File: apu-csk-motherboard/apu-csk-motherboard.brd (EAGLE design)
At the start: 90.2 x 95.9 mm, 9 parts

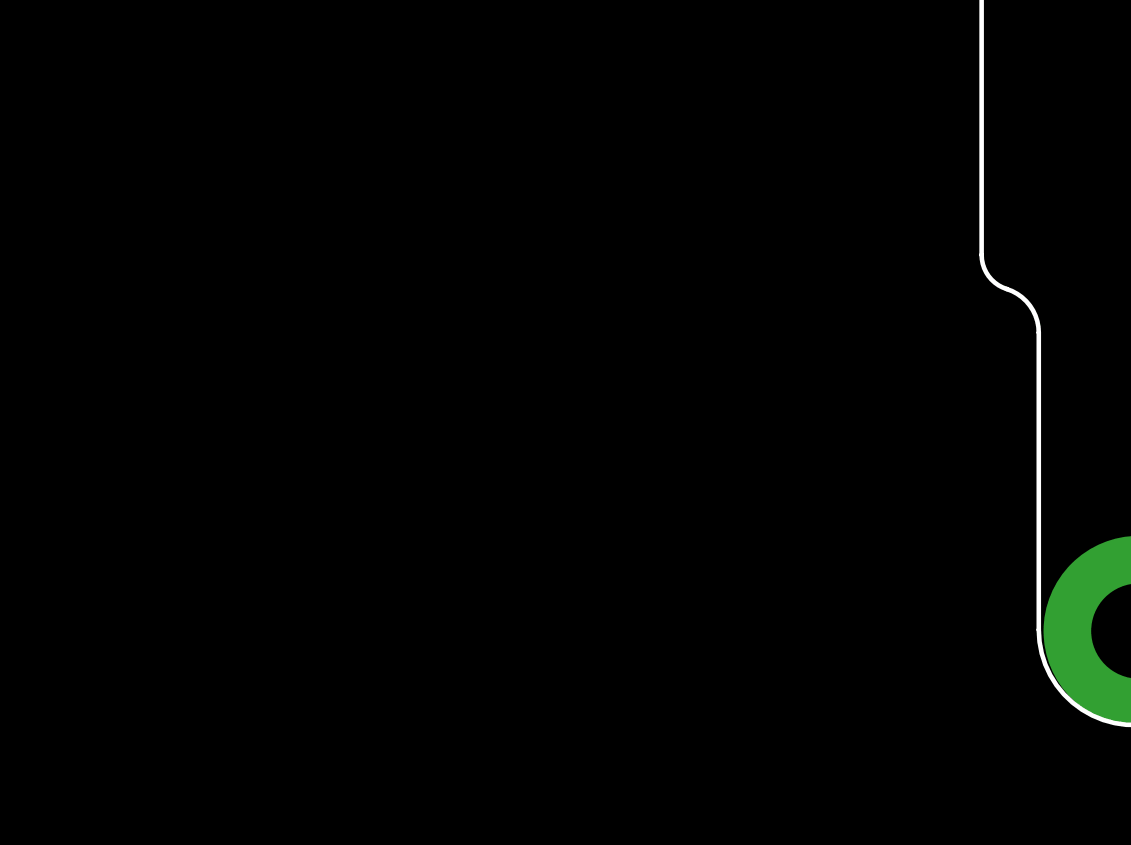
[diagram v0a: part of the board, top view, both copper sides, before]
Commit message: added the sd card schematic to the library
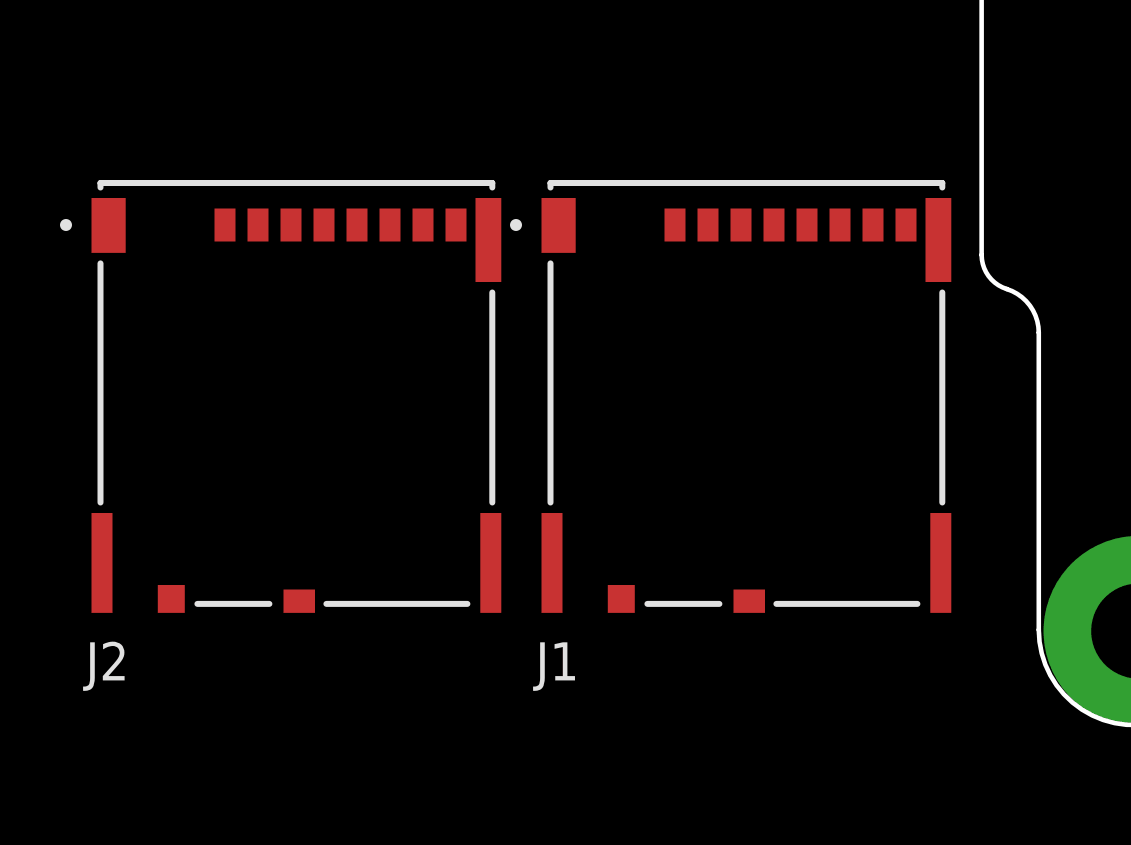
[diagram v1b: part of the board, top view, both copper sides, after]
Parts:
- added J1, J2: MEM2080-00-128-00-A_REVA, MEM2080-00-128-00-A_REVA:GCT_MEM2080-00-128-00-A_REVA
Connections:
- new net VDD: J1.P4, J2.P4
- new net VSS: J1.P6, J2.P6
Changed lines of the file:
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@@
 </layers>
 <board>
-<fusionsync huburn="a.cGVyc29uYWw6dWUyZDI2NzMx" projecturn="a.cGVyc29uYWw6dWUyZDI2NzMxIzIwMjIwOTMwNTYyNjE0OTA2" f3durn="urn:adsk.wipprod:dm.lineage:kB2Wh1Q4TRikTqmI8AqMMA" pcbguid="" lastpulledtime="" lastsyncedchangeguid="" latestrevisionid="4b27a098-c4a4-4352-931e-bf35d80debb3" lastsyncedrevisionid="4b27a098-c4a4-4352-931e-bf35d80debb3" lastboardhashguid="35456882-ee58-db46-62f4-8c871885f9ca" lastpushedtime="2022-10-02T03:41:01Z" linktopcb3d="true"/>
+<fusionsync huburn="a.cGVyc29uYWw6dWUyZDI2NzMx" projecturn="a.cGVyc29uYWw6dWUyZDI2NzMxIzIwMjIwOTMwNTYyNjE0OTA2" f3durn="urn:adsk.wipprod:dm.lineage:kB2Wh1Q4TRikTqmI8AqMMA" pcbguid="" lastpulledtime="" lastsyncedchangeguid="" latestrevisionid="4b27a098-c4a4-4352-931e-bf35d80debb3" lastsyncedrevisionid="4b27a098-c4a4-4352-931e-bf35d80debb3" lastboardhashguid="35456882-ee58-db46-62f4-8c871885f9ca" lastpushedtime="2022-10-02T03:41:01Z" linktopcb3d="false"/>
 <plain>
 <wire x1="39.9699" y1="4.4855" x2="41.4939" y2="2.9615" width="0.1524" layer="20" curve="90" locked="yes"/>
@@
 <attribute name="VALUE" x="0" y="55.75" locked="yes" size="1.27" layer="27"/>
 </element>
+<element name="J1" library="MEM2080-00-128-00-A_REVA" package="GCT_MEM2080-00-128-00-A_REVA" value="MEM2080-00-128-00-A_REVA" x="-8" y="13" smashed="yes">
+<attribute name="AVAILABILITY" value="In Stock" x="-8" y="13" size="1.778" layer="27" display="off"/>
+<attribute name="DESCRIPTION" value=" 9 (8 + 1) Position Card Connector Secure Digital - microSD™ Surface Mount, Right Angle Gold " x="-8" y="13" size="1.778" layer="27" display="off"/>
+<attribute name="MF" value="Global Connector Technology" x="-8" y="13" size="1.778" layer="27" display="off"/>
+<attribute name="MP" value="MEM2080-00-128-00-A" x="-8" y="13" size="1.778" layer="27" display="off"/>
+<attribute name="NAME" x="-15.0292" y="3.4342" size="1.27" layer="25"/>
+<attribute name="PACKAGE" value="None" x="-8" y="13" size="1.778" layer="27" display="off"/>
+<attribute name="PRICE" value="None" x="-8" y="13" size="1.778" layer="27" display="off"/>
+<attribute name="PURCHASE-URL" value="https://pricing.snapeda.com/search/part/MEM2080-00-128-00-A/?ref=eda" x="-8" y="13" size="1.778" layer="27" display="off"/>
+<attribute name="VALUE" x="-14.953" y="2.6316" size="1.27" layer="27" align="top-left"/>
+</element>
+<element name="J2" library="MEM2080-00-128-00-A_REVA" package="GCT_MEM2080-00-128-00-A_REVA" value="MEM2080-00-128-00-A_REVA" x="-23" y="13" smashed="yes">
+<attribute name="AVAILABILITY" value="In Stock" x="-23" y="13" size="1.778" layer="27" display="off"/>
+<attribute name="DESCRIPTION" value=" 9 (8 + 1) Position Card Connector Secure Digital - microSD™ Surface Mount, Right Angle Gold " x="-23" y="13" size="1.778" layer="27" display="off"/>
+<attribute name="MF" value="Global Connector Technology" x="-23" y="13" size="1.778" layer="27" display="off"/>
+<attribute name="MP" value="MEM2080-00-128-00-A" x="-23" y="13" size="1.778" layer="27" display="off"/>
+<attribute name="NAME" x="-30.0292" y="3.4342" size="1.27" layer="25"/>
+<attribute name="PACKAGE" value="None" x="-23" y="13" size="1.778" layer="27" display="off"/>
+<attribute name="PRICE" value="None" x="-23" y="13" size="1.778" layer="27" display="off"/>
+<attribute name="PURCHASE-URL" value="https://pricing.snapeda.com/search/part/MEM2080-00-128-00-A/?ref=eda" x="-23" y="13" size="1.778" layer="27" display="off"/>
+<attribute name="VALUE" x="-29.953" y="2.6316" size="1.27" layer="27" align="top-left"/>
+</element>
 </elements>
 <signals>
@@
 <wire x1="37.9409" y1="21.2852" x2="67.31" y2="83.185" width="0" layer="19" extent="1-1"/>
 </signal>
+<signal name="VDD">
+<contactref element="J1" pad="P4"/>
+<contactref element="J2" pad="P4"/>
+<wire x1="-22.08" y1="18.615" x2="-7.08" y2="18.615" width="0" layer="19" extent="1-1"/>
+</signal>
+<signal name="VSS">
+<contactref element="J1" pad="P6"/>
+<contactref element="J2" pad="P6"/>
+<wire x1="-19.88" y1="18.615" x2="-4.88" y2="18.615" width="0" layer="19" extent="1-1"/>
+</signal>
 </signals>

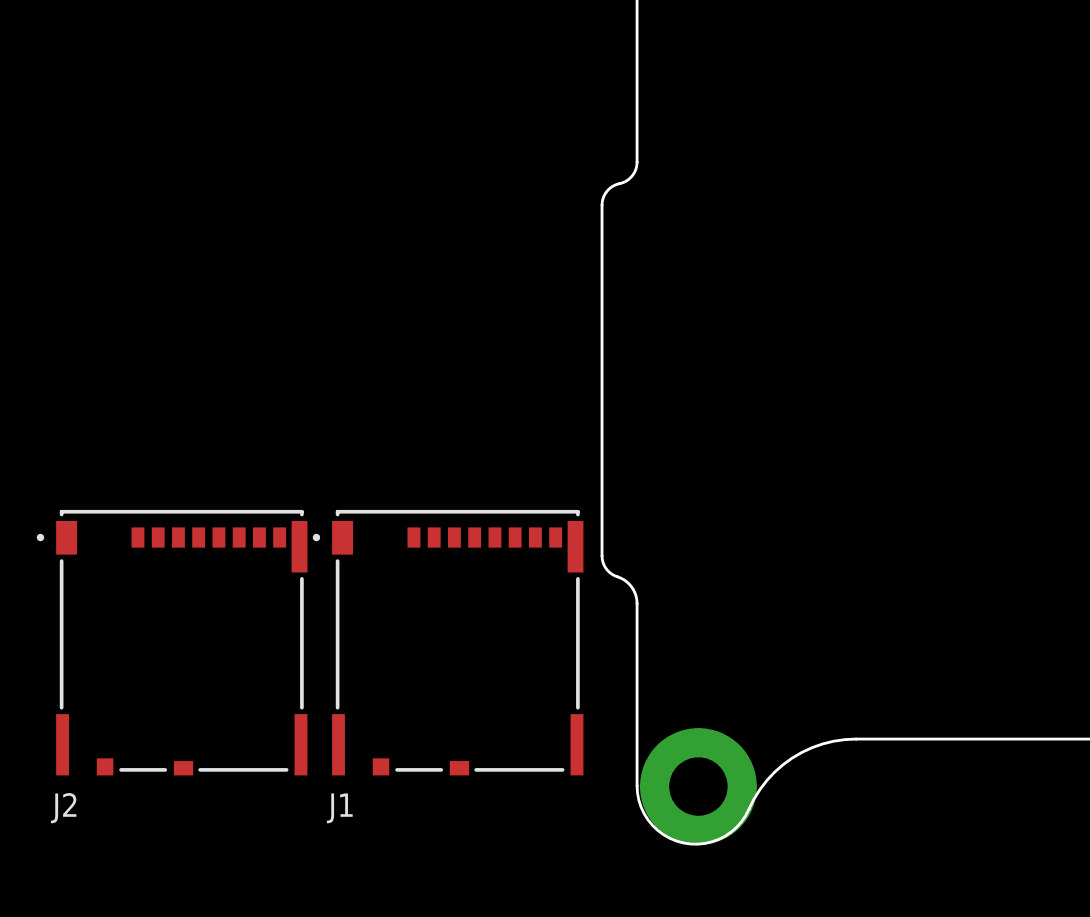
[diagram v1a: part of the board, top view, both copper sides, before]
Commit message: Started Connecting the SD Card to the MicroController
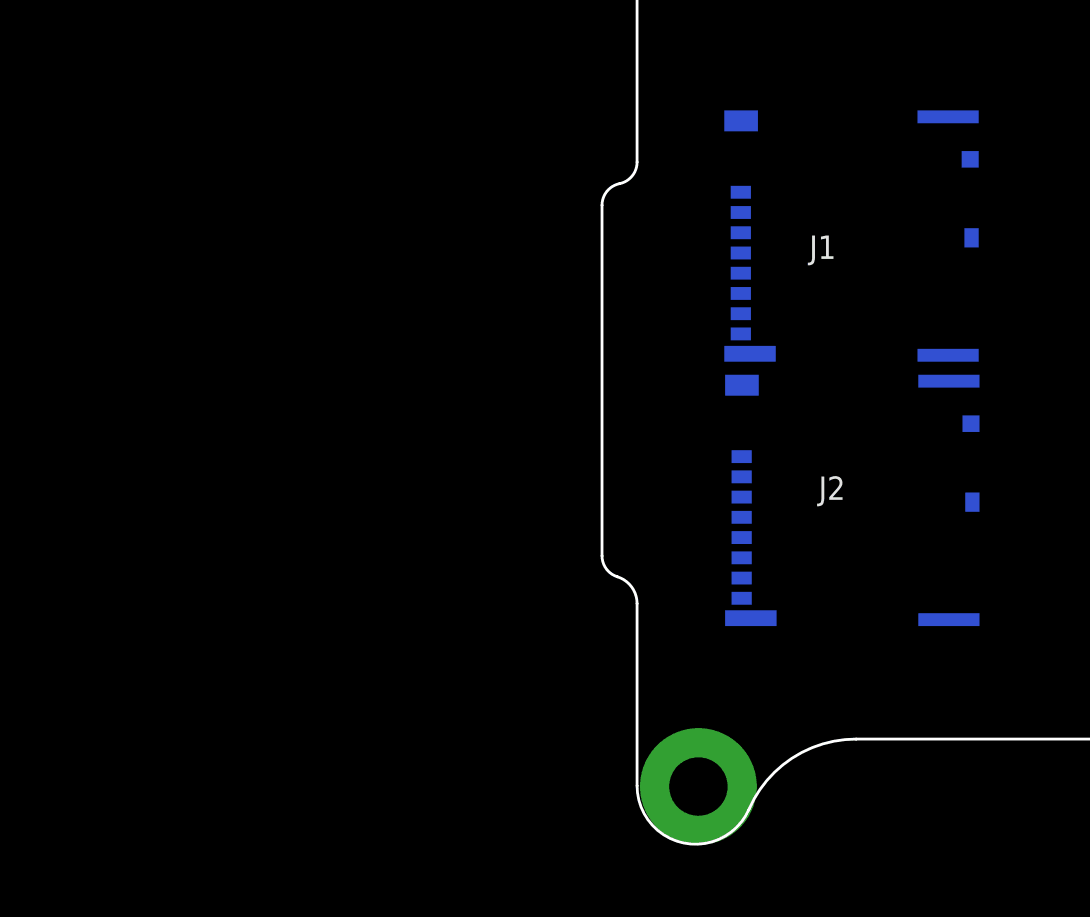
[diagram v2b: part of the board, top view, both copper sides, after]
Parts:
- moved J2 36.8 mm to (13.0, 20.6), flipped to the bottom, turned to 270 degrees
- moved J1 30.4 mm to (13.0, 35.0), flipped to the bottom, turned to 270 degrees
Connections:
- removed net VDD: J1.P4, J2.P4
- removed net VSS: J1.P6, J2.P6
- new net 5V: PL3.1
- new net CS-SD1: J1.P2, J2.P2
- new net DETECT-J1: J1.DSW2
- new net DETECT-J2: J2.DSW2
- new net MISO: FEATHER1.T4, J1.P7, J2.P7
- new net MOSI: FEATHER1.T5, J1.P3, J2.P3
- new net N$1: H1.24
- new net N$2: H1.22
- new net N$3: H1.20
- new net N$4: H1.18
- new net N$5: H1.23
- new net N$7: H1.19
- new net N$8: H1.17
- new net SCK: FEATHER1.T6, H1.21, J1.P5, J2.P5
- new net USER0: H1.47, PL2.7
- new net USER1: H1.48, PL2.9
- new net USER10: H2.51, PL2.27
- new net USER11: H2.52, PL2.29
- new net USER2: H1.49, PL2.11
- new net USER3: H1.50, PL2.13
- new net USER4: H1.51, PL2.15
- new net USER5: H1.52, PL2.17
- new net USER6: H2.47, PL2.19
- new net USER7: H2.48, PL2.21
- new net USER8: H2.49, PL2.23
- new net USER9: H2.50, PL2.25
- net 3.3V: now also J1.P4, J2.P4
- net GND: now also J1.DSW1, J1.P6, J1.S1, J1.S2, J1.S3, J1.S4, J2.DSW1, J2.P6, J2.S1, J2.S2, J2.S3, J2.S4

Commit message: Proper SD Card
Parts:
- removed J1, J2: MEM2080-00-128-00-A_REVA, MEM2080-00-128-00-A_REVA:GCT_MEM2080-00-128-00-A_REVA
- added SD-1, SD-2: 503182-1852, 503182-1852:MOLEX_503182-1852
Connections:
- removed net CS-SD1: J1.P2, J2.P2
- removed net DETECT-J1: J1.DSW2
- removed net DETECT-J2: J2.DSW2
- removed net MISO: FEATHER1.T4, J1.P7, J2.P7
- removed net MOSI: FEATHER1.T5, J1.P3, J2.P3
- new net CIPO: FEATHER1.T4, SD-1.7, SD-2.7
- new net COPI: FEATHER1.T5, SD-1.3, SD-2.3
- new net CS-1: FEATHER1.T12, SD-1.2
- new net CS-2: FEATHER1.T11, SD-2.2
- new net DETECT-1: SD-1.DT
- new net DETECT-2: SD-2.DT
- net 3.3V: now also SD-1.4, SD-2.4; no longer J1.P4, J2.P4
- net GND: now also SD-1.6, SD-1.P1, SD-1.P2, SD-1.P3, SD-1.P4, SD-1.P5, SD-1.SW, SD-2.6, SD-2.P1, SD-2.P2, SD-2.P3, SD-2.P4, SD-2.P5, SD-2.SW; no longer J1.DSW1, J1.P6, J1.S1, J1.S2, J1.S3, J1.S4, J2.DSW1, J2.P6, J2.S1, J2.S2, J2.S3, J2.S4
- net SCK: now also SD-1.5, SD-2.5; no longer J1.P5, J2.P5

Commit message: Corrected the Detect and Swith on the SD Card
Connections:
- removed net DETECT-1: SD-1.DT
- removed net DETECT-2: SD-2.DT
- removed net N$1: H1.24
- new net CS-FPGA: FEATHER1.T9, PL3.4
- new net CS-SD: FEATHER1.T10, H1.24
- new net UC_RXO: FEATHER1.T3, PL3.8
- new net UC_TXO: FEATHER1.T2, PL3.6
- net GND: no longer SD-1.SW, SD-2.SW
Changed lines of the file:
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@@
 <contactref element="SD-2" pad="P4"/>
 <contactref element="SD-2" pad="6"/>
-<contactref element="SD-2" pad="SW"/>
 <contactref element="SD-1" pad="P3"/>
 <contactref element="SD-1" pad="P5"/>
@@
 <contactref element="SD-1" pad="P2"/>
 <contactref element="SD-1" pad="P4"/>
-<contactref element="SD-1" pad="SW"/>
 <contactref element="SD-1" pad="6"/>
 <wire x1="52.07" y1="88.265" x2="52.07" y2="90.805" width="0" layer="19" extent="1-1"/>
@@
 <wire x1="6.013" y1="76" x2="49.53" y2="88.265" width="0" layer="19" extent="1-1"/>
 <wire x1="2" y1="59" x2="6.013" y2="76" width="0" layer="19" extent="1-1"/>
-<wire x1="35.4009" y1="41.6052" x2="2" y2="59" width="0" layer="19" extent="1-1"/>
-<wire x1="65.8809" y1="41.6052" x2="35.4009" y2="41.6052" width="0" layer="19" extent="1-1"/>
-<wire x1="5.125" y1="54.145" x2="35.4009" y2="41.6052" width="0" layer="19" extent="1-1"/>
-<wire x1="7.275" y1="53.74" x2="5.125" y2="54.145" width="0" layer="19" extent="1-1"/>
+<wire x1="5.125" y1="54.145" x2="2" y2="59" width="0" layer="19" extent="1-1"/>
 <wire x1="4.645" y1="49.6" x2="5.125" y2="54.145" width="0" layer="19" extent="1-1"/>
 <wire x1="5.275" y1="39.755" x2="4.645" y2="49.6" width="0" layer="19" extent="1-1"/>
-<wire x1="17.4" y1="51.94" x2="7.275" y2="53.74" width="0" layer="19" extent="1-1"/>
-<wire x1="4.645" y1="31.6" x2="17.4" y2="51.94" width="0" layer="19" extent="1-1"/>
-<wire x1="5.125" y1="36.145" x2="4.645" y2="31.6" width="0" layer="19" extent="1-1"/>
-<wire x1="7.275" y1="35.74" x2="5.125" y2="36.145" width="0" layer="19" extent="1-1"/>
-<wire x1="17.4" y1="44.16" x2="4.645" y2="31.6" width="0" layer="19" extent="1-1"/>
-<wire x1="16.605" y1="39.855" x2="17.4" y2="44.16" width="0" layer="19" extent="1-1"/>
-<wire x1="5.275" y1="21.755" x2="16.605" y2="39.855" width="0" layer="19" extent="1-1"/>
-<wire x1="17.4" y1="33.94" x2="7.275" y2="35.74" width="0" layer="19" extent="1-1"/>
+<wire x1="5.125" y1="36.145" x2="5.275" y2="39.755" width="0" layer="19" extent="1-1"/>
+<wire x1="4.645" y1="31.6" x2="5.125" y2="36.145" width="0" layer="19" extent="1-1"/>
+<wire x1="5.275" y1="21.755" x2="4.645" y2="31.6" width="0" layer="19" extent="1-1"/>
+<wire x1="16.605" y1="39.855" x2="5.275" y2="39.755" width="0" layer="19" extent="1-1"/>
+<wire x1="17.4" y1="44.16" x2="16.605" y2="39.855" width="0" layer="19" extent="1-1"/>
+<wire x1="17.4" y1="33.94" x2="16.605" y2="39.855" width="0" layer="19" extent="1-1"/>
+<wire x1="17.4" y1="51.94" x2="17.4" y2="44.16" width="0" layer="19" extent="1-1"/>
 <wire x1="17.4" y1="26.16" x2="17.4" y2="33.94" width="0" layer="19" extent="1-1"/>
 <wire x1="16.605" y1="21.855" x2="17.4" y2="26.16" width="0" layer="19" extent="1-1"/>
+<wire x1="35.4009" y1="41.6052" x2="17.4" y2="44.16" width="0" layer="19" extent="1-1"/>
+<wire x1="65.8809" y1="41.6052" x2="35.4009" y2="41.6052" width="0" layer="19" extent="1-1"/>
 </signal>
 <signal name="3.3V">
@@
 <wire x1="4.645" y1="30.5" x2="4.645" y2="48.5" width="0" layer="19" extent="1-1"/>
 </signal>
-<signal name="N$1">
-<contactref element="H1" pad="24"/>
-</signal>
 <signal name="N$2">
 <contactref element="H1" pad="22"/>
@@
 <signal name="N$8">
 <contactref element="H1" pad="17"/>
-</signal>
-<signal name="DETECT-1">
-<contactref element="SD-1" pad="DT"/>
 </signal>
 <signal name="CS-1">
@@
 <wire x1="4.645" y1="32.7" x2="4.645" y2="50.7" width="0" layer="19" extent="1-1"/>
 </signal>
-<signal name="DETECT-2">
-<contactref element="SD-2" pad="DT"/>
+<signal name="CS-SD">
+<contactref element="FEATHER1" pad="T10"/>
+<contactref element="H1" pad="24"/>
+<wire x1="58.2609" y1="41.6052" x2="41.91" y2="85.725" width="0" layer="19" extent="1-1"/>
+</signal>
+<signal name="UC_RXO">
+<contactref element="FEATHER1" pad="T3"/>
+<contactref element="PL3" pad="8"/>
+<wire x1="8.02" y1="59" x2="40.4809" y2="41.6052" width="0" layer="19" extent="1-1"/>
+</signal>
+<signal name="UC_TXO">
+<contactref element="FEATHER1" pad="T2"/>
+<contactref element="PL3" pad="6"/>
+<wire x1="6.013" y1="59" x2="37.9409" y2="41.6052" width="0" layer="19" extent="1-1"/>
+</signal>
+<signal name="CS-FPGA">
+<contactref element="FEATHER1" pad="T9"/>
+<contactref element="PL3" pad="4"/>
+<wire x1="4.007" y1="59" x2="55.7209" y2="41.6052" width="0" layer="19" extent="1-1"/>
 </signal>
 </signals>
